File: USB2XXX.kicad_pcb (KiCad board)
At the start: 2 copper layers, 58.7 x 34.3 mm, 63 parts, among them J1 Conn_01x04, J2 Conn_01x03, J3 Conn_01x03, J4 Conn_01x02, J5 Conn_01x02, Q1 S8050, U1 STM32F072C8Tx, U2 TJA1051T-3, U3 HX9193, U4 STM32F072C8Tx, U5 TJA1051T-3, U6 SL2.1S, U7 CH340E, U8 CH340E, Y1 12M

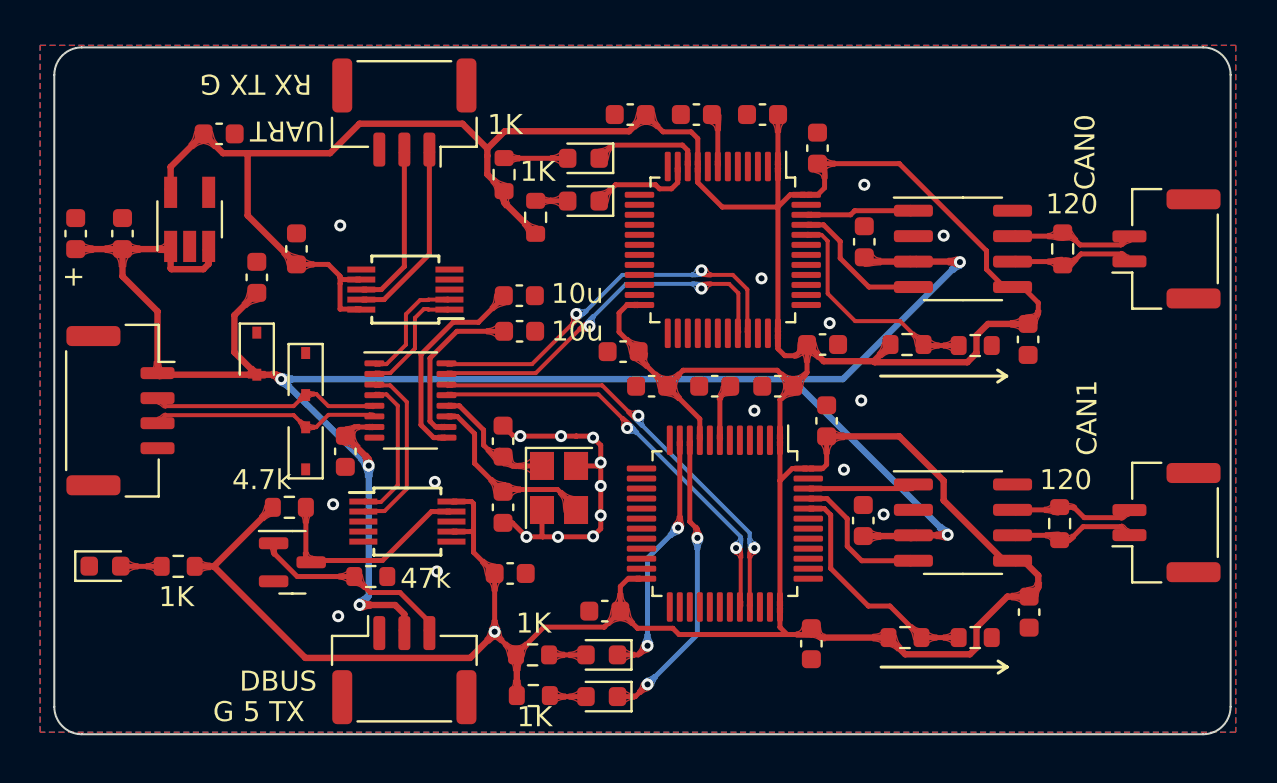
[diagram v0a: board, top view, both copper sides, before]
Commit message: Big update on UART-pilot lamp/routings/connectors/esd protection
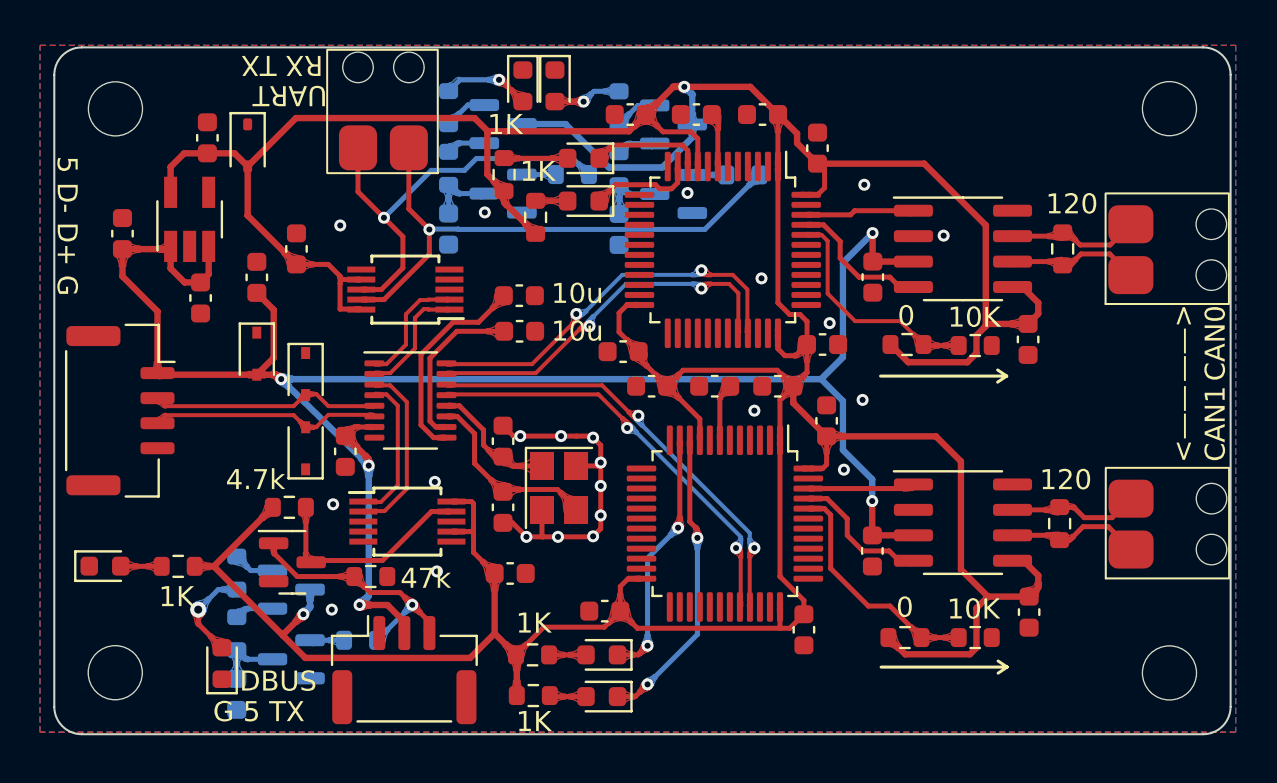
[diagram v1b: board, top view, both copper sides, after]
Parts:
- added C28: 1u, Capacitor_SMD:C_0603_1608Metric, B.Cu at (105.3, 65.7)
- added C29: 1u, Capacitor_SMD:C_0603_1608Metric, B.Cu at (113.8, 65.7)
- added C30: 1u, Capacitor_SMD:C_0603_1608Metric, B.Cu at (94.8, 88.9)
- added D10: LED, LED_SMD:LED_0603_1608Metric, F.Cu at (110.6, 58.5)
- added D11: LED, LED_SMD:LED_0603_1608Metric, F.Cu at (94.0, 87.3)
- added D12: BV05C, Diode_SMD:D_SOD-323, F.Cu at (95.3, 61.5)
- added D9: LED, LED_SMD:LED_0603_1608Metric, F.Cu at (109.0, 58.5)
- added H1: MountingHole, MountingHole:MountingHole_2.7mm_M2.5, F.Cu at (141.3, 59.6)
- added H2: MountingHole, MountingHole:MountingHole_2.7mm_M2.5, F.Cu at (88.7, 87.8)
- added H3: MountingHole, MountingHole:MountingHole_2.7mm_M2.5, F.Cu at (141.3, 87.8)
- added H4: MountingHole, MountingHole:MountingHole_2.7mm_M2.5, F.Cu at (88.7, 59.7)
- added Q2: Q_PNP_BCE, Package_TO_SOT_SMD:SOT-23, B.Cu at (108.1, 63.9)
- added Q3: Q_PNP_BCE, Package_TO_SOT_SMD:SOT-23, B.Cu at (108.1, 60.4)
- added Q4: Q_PNP_BCE, Package_TO_SOT_SMD:SOT-23, B.Cu at (116.6, 63.9)
- added Q5: Q_PNP_BCE, Package_TO_SOT_SMD:SOT-23, B.Cu at (116.6, 60.4)
- added Q6: Q_PNP_BCE, Package_TO_SOT_SMD:SOT-23, B.Cu at (97.5, 87.1)
- added Q7: Q_PNP_BCE, Package_TO_SOT_SMD:SOT-23, B.Cu at (97.5, 83.7)
- added R15: 1K, Resistor_SMD:R_0603_1608Metric, B.Cu at (111.5, 62.9)
- added R16: 1K, Resistor_SMD:R_0603_1608Metric, B.Cu at (105.3, 62.6)
- added R17: 240, Resistor_SMD:R_0603_1608Metric, B.Cu at (105.3, 59.6)
- added R18: 1K, Resistor_SMD:R_0603_1608Metric, B.Cu at (120.0, 63.0)
- added R19: 1K, Resistor_SMD:R_0603_1608Metric, B.Cu at (113.8, 62.6)
- added R20: 240, Resistor_SMD:R_0603_1608Metric, B.Cu at (113.8, 59.6)
- added R21: 1K, Resistor_SMD:R_0603_1608Metric, B.Cu at (100.9, 86.2)
- added R22: 1K, Resistor_SMD:R_0603_1608Metric, B.Cu at (94.8, 85.9)
- added R23: 240, Resistor_SMD:R_0603_1608Metric, B.Cu at (94.8, 82.8)
- D1, D2: value LED -> BLUE
- D3, D4: value LED -> RED
- D8: value LED -> GREEN
- J3: value Conn_01x03 -> Conn_01x02; footprint Connector_JST:JST_GH_SM03B-GHS-TB_1x03-1MP_P1.25mm_Horizontal -> Connector:MountingHole_0.8mm_sm2.5_2pin
- J4, J5: footprint Connector_JST:JST_GH_SM02B-GHS-TB_1x02-1MP_P1.25mm_Horizontal -> Connector:MountingHole_0.8mm_sm2.5_2pin
- moved C9 7.01 mm to (93.0, 69.1), turned to -90 degrees
- moved C23 1.82 mm to (126.5, 68.1), turned to -90 degrees
- moved C27 1.58 mm to (126.5, 81.7), turned to -90 degrees
- moved J3 1.17 mm to (102.1, 59.3)
- moved C15 0.79 mm to (123.1, 85.7)
- moved C4 0.62 mm to (93.3, 61.1), turned to 90 degrees
- moved J5 0.52 mm to (141.7, 80.4)
- moved J4 0.51 mm to (141.7, 66.7)
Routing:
- net /UART/RXD: track 9.41 -> 27.7 mm, vias 0 -> 1
- net VCC: track 219.9 -> 237.7 mm, vias 1 -> 2
- net /UART/TXD: track 8.31 -> 21.2 mm, vias 0 -> 1
- net +5V: track 103.9 -> 95.0 mm
- net Net-(D11-A): track 0.00 -> 4.73 mm, vias 0 -> 1
- net Net-(D9-A): track 0.00 -> 4.39 mm, vias 0 -> 1
- net Net-(D10-A): track 0.00 -> 3.42 mm, vias 0 -> 1
- net Net-(Q6-E): track 0.00 -> 3.40 mm
- net Net-(Q2-E): track 0.00 -> 3.39 mm
- net Net-(Q4-E): track 0.00 -> 3.39 mm
- net /DBUS/DBus: track 10.2 -> 12.7 mm, vias 0 -> 1
- net Net-(Q3-C): track 0.00 -> 2.18 mm
- net Net-(Q5-C): track 0.00 -> 2.17 mm
- net Net-(Q7-C): track 0.00 -> 2.07 mm
- net Net-(Q3-B): track 0.00 -> 1.96 mm
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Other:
- board text added: "0"
- board text added: "10K"
- board text added: "1u"
- board text added: "240"
- board text added: "5 D- D+ G"
- board text added: "<—— CAN1"
- board text added: "RX TX"
- board text added: "——> CAN0"
- board text removed: "+"
- board text removed: "CAN0"
- board text removed: "CAN1"
- board text removed: "RX TX G"

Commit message: Change connectors back to GH1.25&Add ESD for UART and CAN
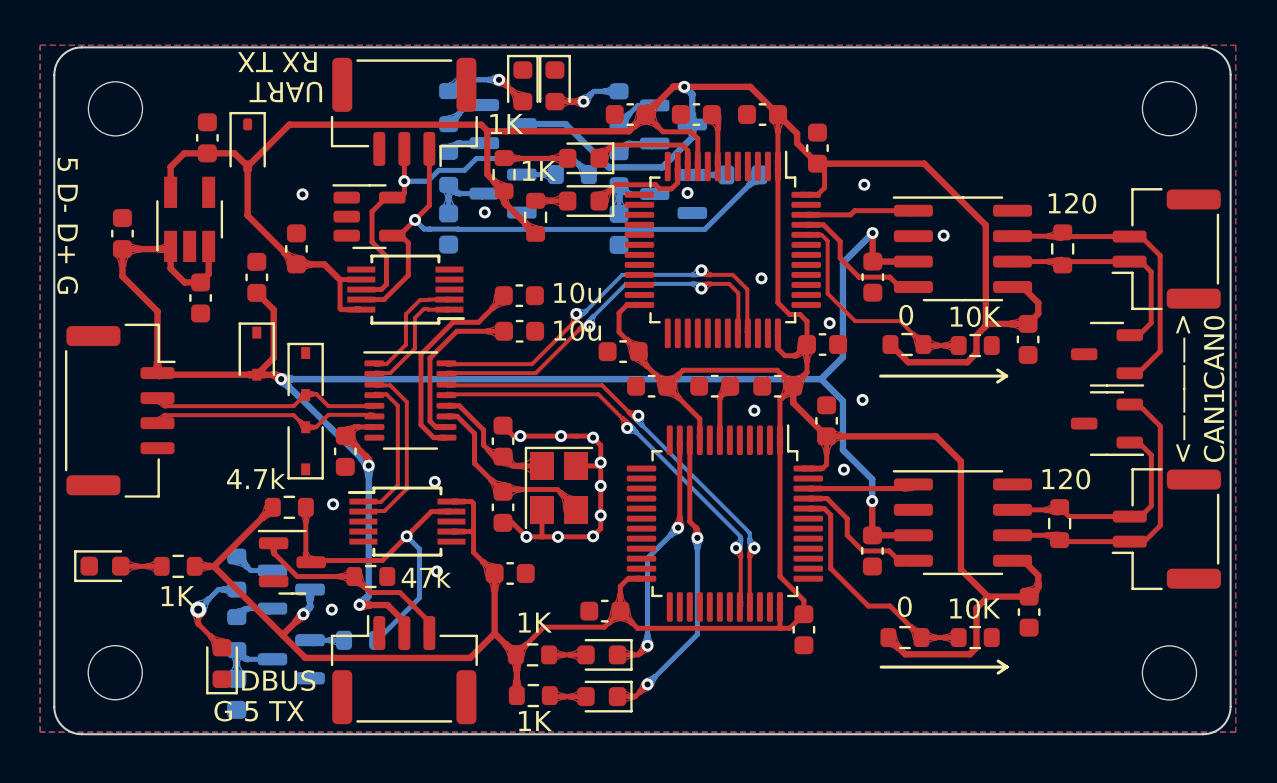
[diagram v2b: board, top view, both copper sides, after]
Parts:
- added U10: ~, Package_TO_SOT_SMD:SOT-23-3, F.Cu at (138.2, 71.9)
- added U11: ~, Package_TO_SOT_SMD:SOT-23-3, F.Cu at (138.2, 75.4)
- added U9: ~, Package_TO_SOT_SMD:SOT-23-5, F.Cu at (101.4, 65.0)
- D12: value BV05C -> BV03C
- J3: value Conn_01x02 -> Conn_01x03; footprint Connector:MountingHole_0.8mm_sm2.5_2pin -> Connector_JST:JST_GH_SM03B-GHS-TB_1x03-1MP_P1.25mm_Horizontal
- J4, J5: footprint Connector:MountingHole_0.8mm_sm2.5_2pin -> Connector_JST:JST_GH_SM02B-GHS-TB_1x02-1MP_P1.25mm_Horizontal
- moved J3 1.15 mm to (103.1, 59.8)
- moved J5 0.56 mm to (141.2, 80.6)
- moved J4 0.50 mm to (141.2, 66.7)
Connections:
- R21 pad 1: /DBUS/DBus -> Net-(Q1-C)
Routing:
- net /STM2_CAN/CAN_L: track 6.77 -> 14.8 mm
- net /STM1_CAN/CAN_H: track 6.68 -> 14.7 mm
- net Net-(Q1-C): track 10.9 -> 17.2 mm, vias 0 -> 1
- net /STM2_CAN/CAN_H: track 6.59 -> 11.3 mm
- net /STM1_CAN/CAN_L: track 6.66 -> 11.2 mm
- net /DBUS/DBus: track 12.7 -> 10.2 mm, vias 1 -> 0
- net /UART/TXD: track 21.2 -> 19.5 mm
- net /UART/RXD: track 27.7 -> 29.3 mm

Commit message: Adaption for SMT
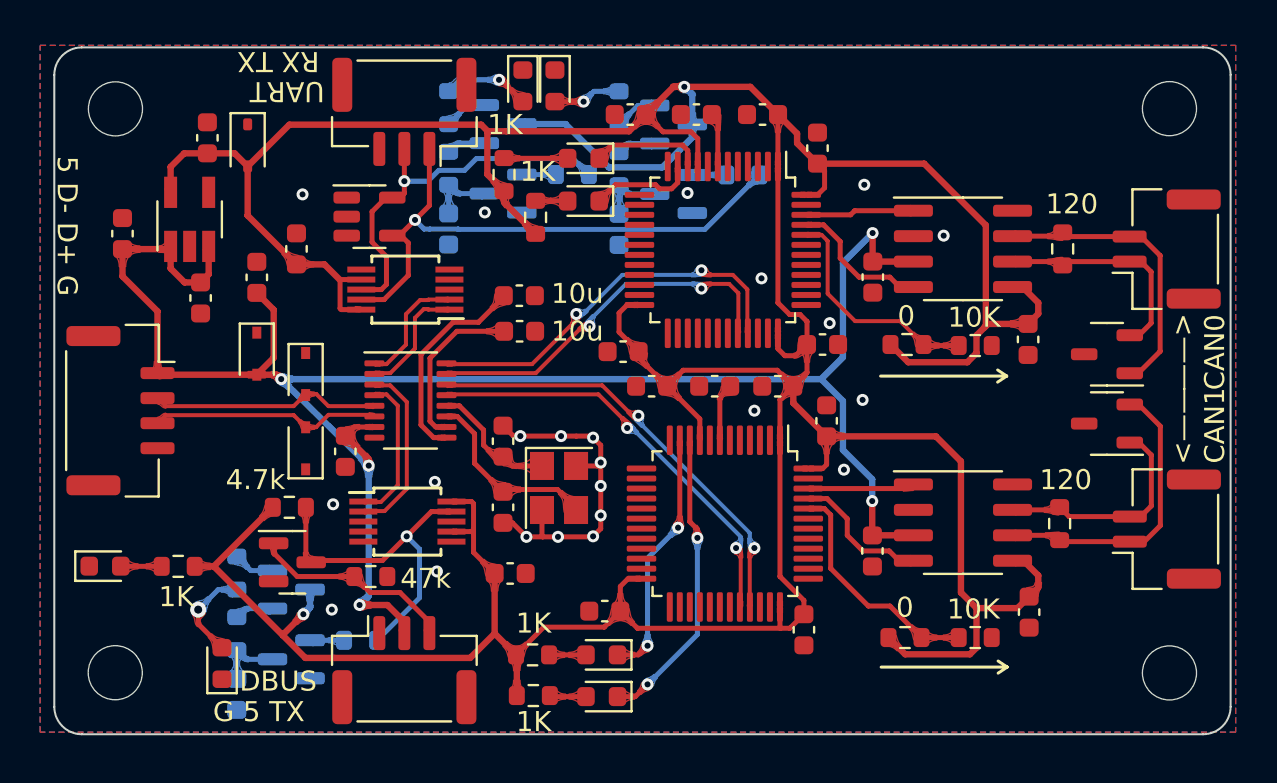
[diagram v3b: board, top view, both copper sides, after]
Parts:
- D10: value LED -> GREEN
- D11: value LED -> YELLOW
- D9: value LED -> RED

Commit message: Adaption for SMT(hotfix)
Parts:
- U10, U11: value ~ -> PESD1CAN
- U9: value ~ -> ESDS314
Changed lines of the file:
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@@
   (net 126 "unconnected-(U8-TNOW-Pad6)")
   (net 127 "unconnected-(U8-TXD-Pad8)")
-  (net 128 "unconnected-(U9-NC-Pad1)")
-  (net 129 "unconnected-(U9-NC-Pad3)")
+  (net 128 "unconnected-(U9-I{slash}O1-Pad1)")
+  (net 129 "unconnected-(U9-I{slash}O2-Pad3)")
   (footprint "LED_SMD:LED_0603_1608Metric" (layer "F.Cu")
     (at 112.9792 89.0016 180)
@@
         (effects (font (size 1 1) (thickness 0.15)))
     )
-    (fp_text value "~" (at 0 2.4) (layer "F.Fab")
+    (fp_text value "PESD1CAN" (at 0 2.4) (layer "F.Fab")
         (effects (font (size 1 1) (thickness 0.15)))
     )
@@
         (effects (font (size 1 1) (thickness 0.15)))
     )
-    (fp_text value "~" (at 0 2.4) (layer "F.Fab")
+    (fp_text value "PESD1CAN" (at 0 2.4) (layer "F.Fab")
         (effects (font (size 1 1) (thickness 0.15)))
     )
@@
         (effects (font (size 1 1) (thickness 0.15)))
     )
-    (fp_text value "~" (at 0 2.4) (layer "F.Fab")
+    (fp_text value "ESDS314" (at 0 2.4) (layer "F.Fab")
         (effects (font (size 1 1) (thickness 0.15)))
     )
@@
       (stroke (width 0.1) (type solid)) (layer "F.Fab"))
     (pad "1" smd roundrect (at -1.1375 -0.95) (size 1.325 0.6) (layers "F.Cu" "F.Paste" "F.Mask") (roundrect_rratio 0.25)
-      (net 128 "unconnected-(U9-NC-Pad1)") (pinfunction "NC") (pintype "no_connect"))
+      (net 128 "unconnected-(U9-I{slash}O1-Pad1)") (pinfunction "I/O1") (pintype "bidirectional+no_connect"))
     (pad "2" smd roundrect (at -1.1375 0) (size 1.325 0.6) (layers "F.Cu" "F.Paste" "F.Mask") (roundrect_rratio 0.25)
       (net 2 "GND") (pinfunction "GND") (pintype "power_out"))
     (pad "3" smd roundrect (at -1.1375 0.95) (size 1.325 0.6) (layers "F.Cu" "F.Paste" "F.Mask") (roundrect_rratio 0.25)
-      (net 129 "unconnected-(U9-NC-Pad3)") (pinfunction "NC") (pintype "no_connect"))
+      (net 129 "unconnected-(U9-I{slash}O2-Pad3)") (pinfunction "I/O2") (pintype "bidirectional+no_connect"))
     (pad "4" smd roundrect (at 1.1375 0.95) (size 1.325 0.6) (layers "F.Cu" "F.Paste" "F.Mask") (roundrect_rratio 0.25)
-      (net 22 "/UART/RXD") (pinfunction "I/O1") (pintype "bidirectional"))
+      (net 22 "/UART/RXD") (pinfunction "I/O3") (pintype "bidirectional"))
     (pad "5" smd roundrect (at 1.1375 -0.95) (size 1.325 0.6) (layers "F.Cu" "F.Paste" "F.Mask") (roundrect_rratio 0.25)
-      (net 23 "/UART/TXD") (pinfunction "I/O2") (pintype "bidirectional"))
+      (net 23 "/UART/TXD") (pinfunction "I/O4") (pintype "bidirectional"))
     (model "${KICAD6_3DMODEL_DIR}/Package_TO_SOT_SMD.3dshapes/SOT-23-5.wrl"
       (offset (xyz 0 0 0))
